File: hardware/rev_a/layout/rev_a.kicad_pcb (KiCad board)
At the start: 4 copper layers, 78 x 58 mm, 68 parts, among them J1 TSW-110-07-T-D, J2 TSW-110-07-T-D, U1 ADS1299-4PAGR, U2 TPS7A2033PDBVR

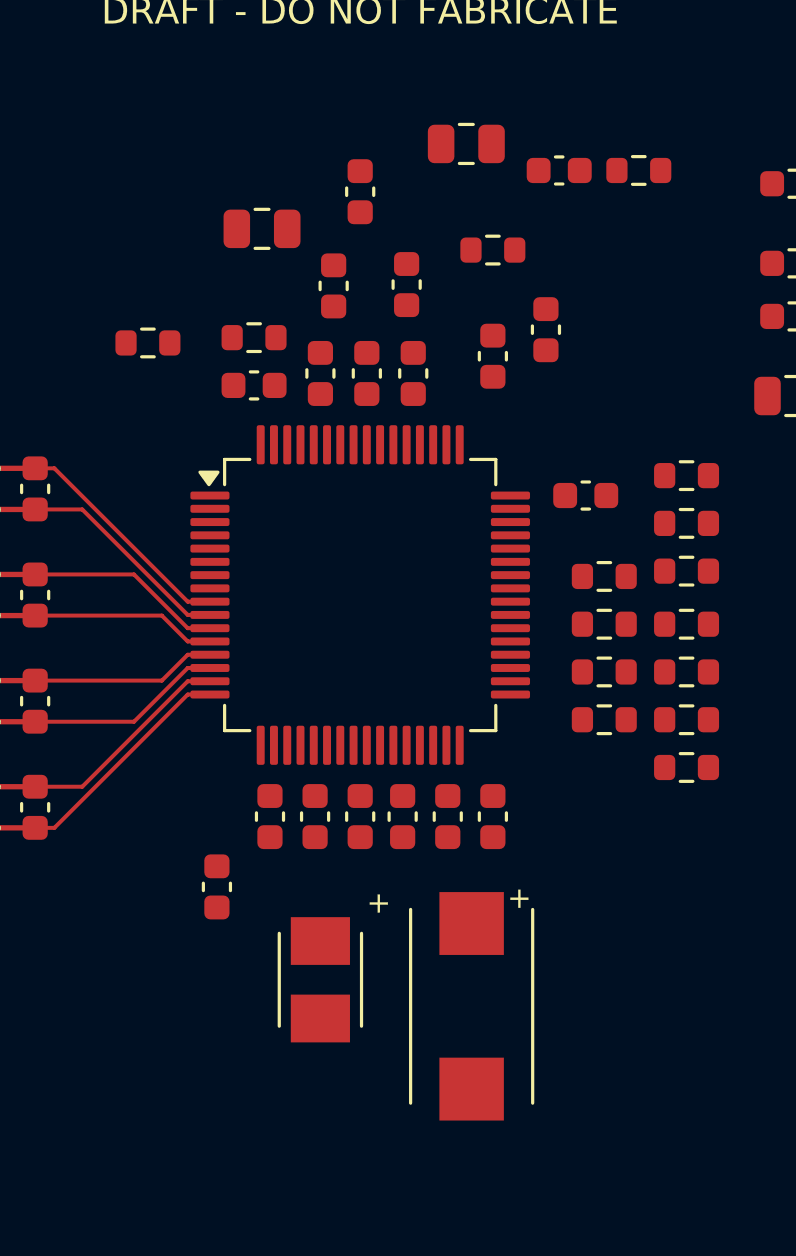
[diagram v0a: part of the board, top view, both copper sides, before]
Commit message: feat(hardware): route local reference and VCAP capacitor networks
Complete the five sensitive positive nets on front copper and add explicit local capacitor return traces. Preserve existing ADC-side routing, schematic, BOM and all approval flags. Two previously unrouted capacitors move for locality/clearance. Native cut-trace and cut-return controls pass; the full local gate remains to be executed on this commit. This is reconstructed local history, not a published GitHub head.
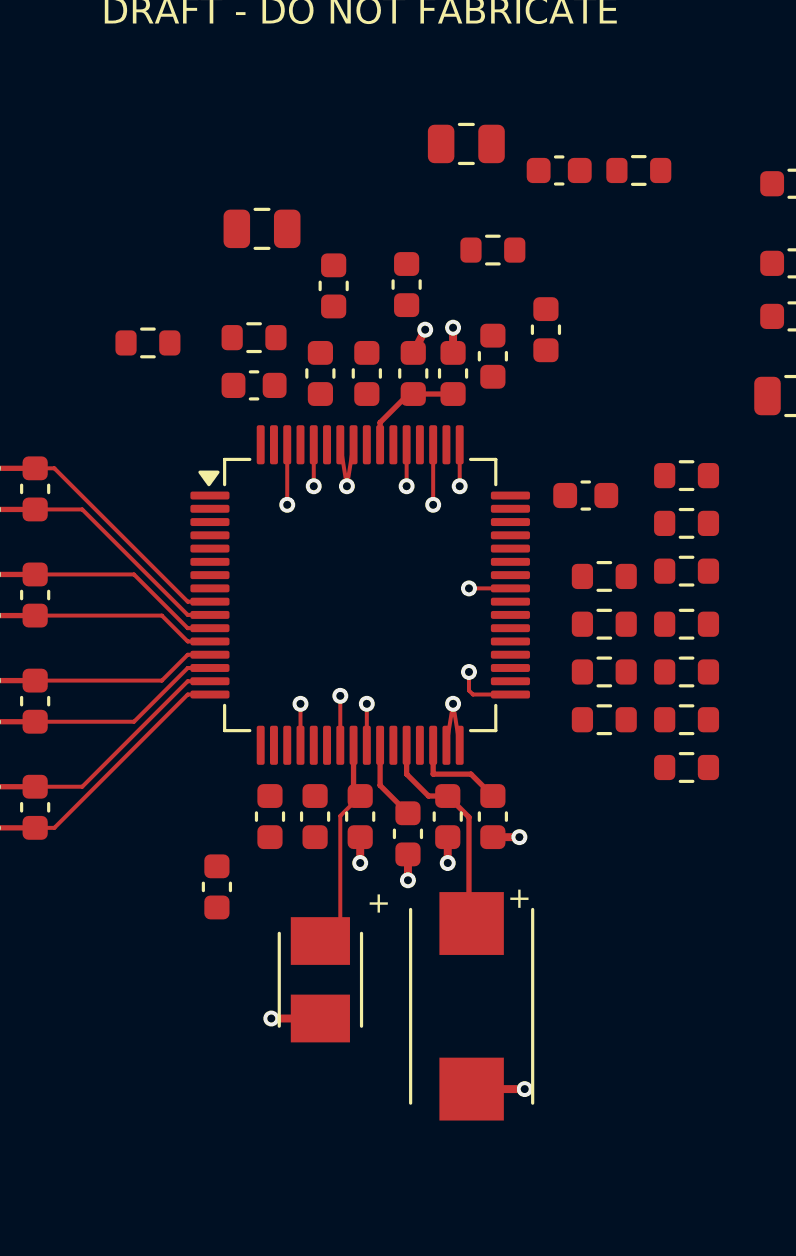
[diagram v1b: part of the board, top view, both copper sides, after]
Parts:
- moved C24 7.69 mm to (51.5, 28.6)
- moved C10 0.68 mm to (49.8, 46.0)
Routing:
- net GND: track 0.00 -> 158.7 mm, vias 0 -> 20
- net VCAP1: track 0.00 -> 8.16 mm
- net VREFP: track 0.00 -> 8.10 mm
- net VCAP3: track 0.00 -> 4.03 mm
- net VCAP2: track 0.00 -> 3.68 mm
- net VCAP4: track 0.00 -> 3.00 mm

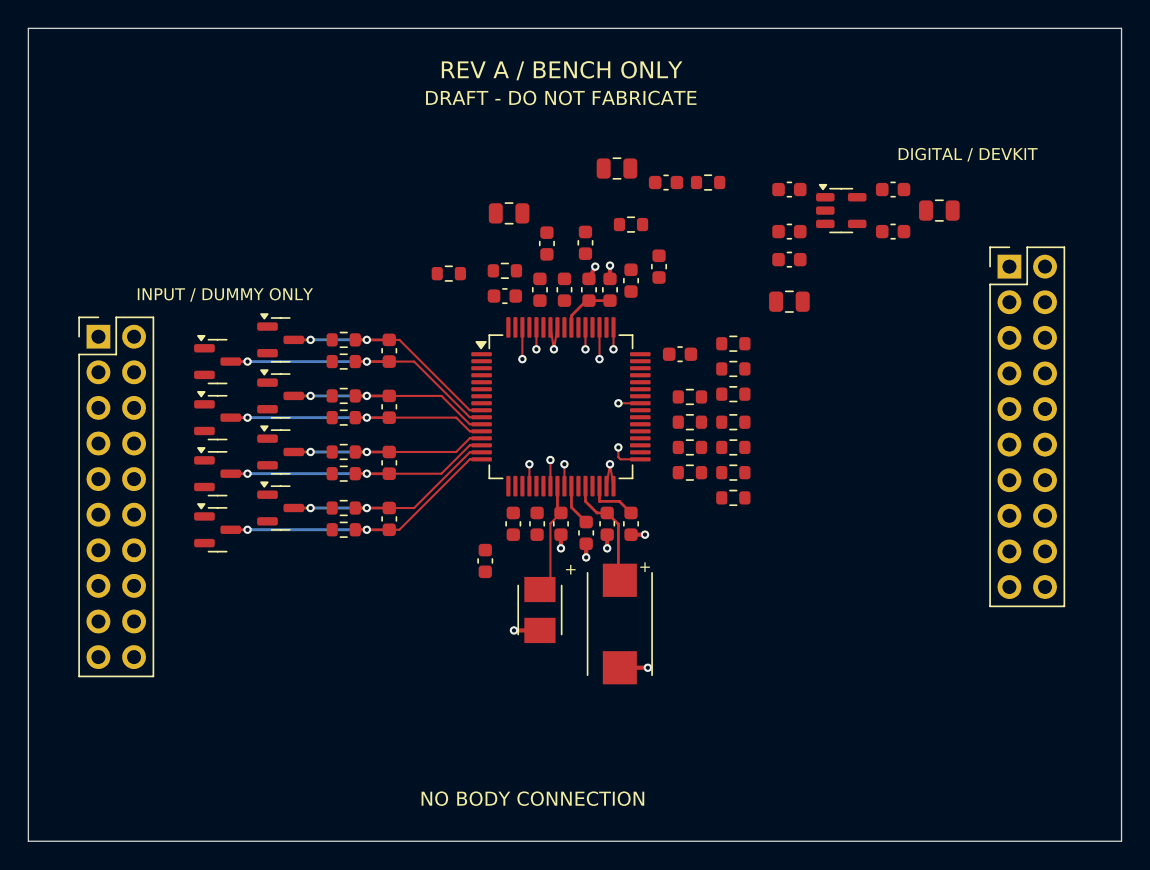
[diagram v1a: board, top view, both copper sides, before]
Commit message: feat(hardware): connect native ground plane and supply routes
Rebuild only the missing post-reference routing: one actual KiCad-filled In1 ground region and distinct VIN, AVDD and DVDD routes. Preserve all component data and existing copper. Canonical native DRC has zero parity/other findings and 35 deliberately unfinished connections. Require actual refill before testing each mutated board, reject missing/clipped planes and cut supply traces, and bind the new test source in the existing snapshot. No physical, purchasing, BOM, circuit, firmware, model or dependency change; full final local gate follows on this commit.
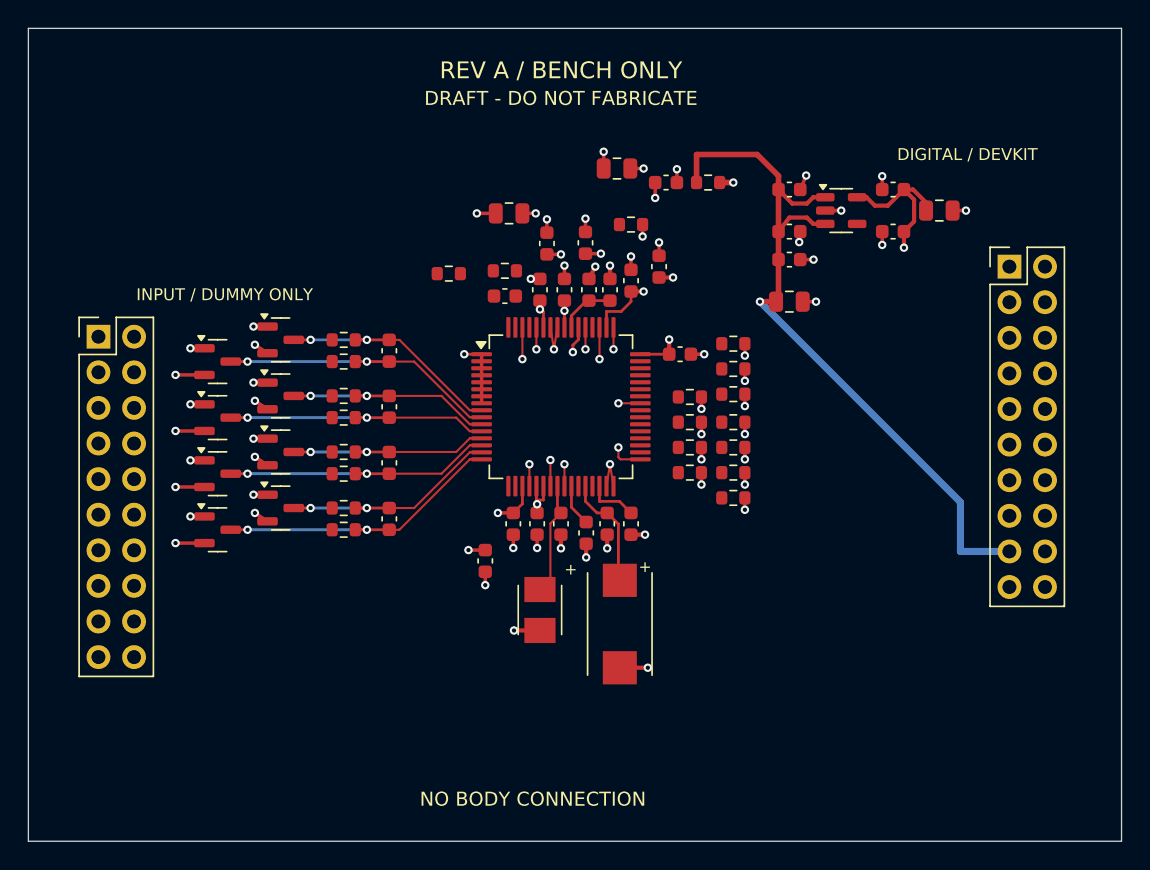
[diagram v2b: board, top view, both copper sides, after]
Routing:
- net AVDD: track 0.00 -> 244.6 mm, vias 0 -> 21
- net VIN_5V_AFE: track 0.00 -> 54.0 mm, vias 0 -> 1
- net DVDD: track 0.00 -> 49.7 mm, vias 0 -> 4
- net GND: track 158.7 -> 196.6 mm, vias 20 -> 61
- added copper zone on In1.Cu, net GND

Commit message: feat(hardware): complete the remaining PCB signal routing draft
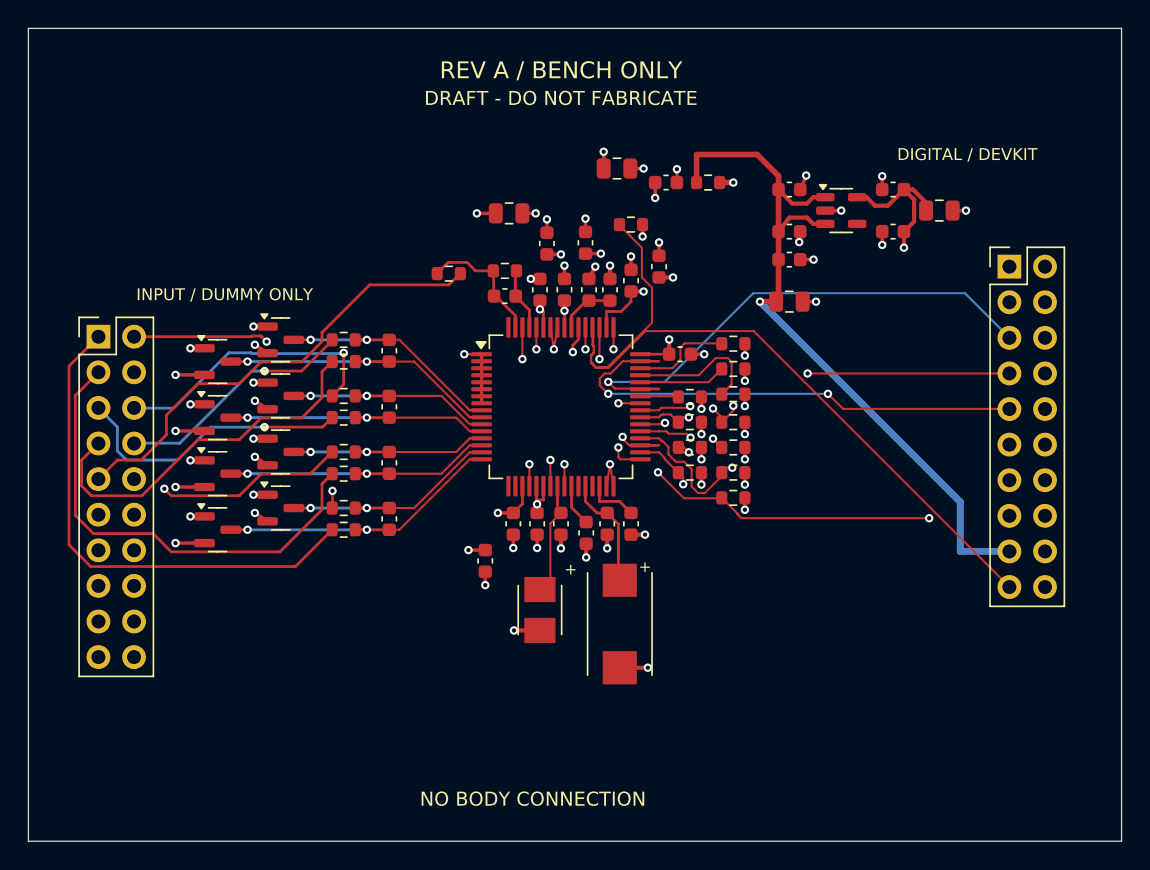
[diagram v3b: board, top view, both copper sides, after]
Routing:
- net CLKSEL: track 0.00 -> 57.7 mm
- net MISO: track 0.00 -> 37.7 mm, vias 0 -> 1
- net DRDY: track 0.00 -> 36.5 mm, vias 0 -> 2
- net CH1P_DUMMY: track 0.00 -> 36.3 mm
- net PWDN: track 0.00 -> 34.4 mm, vias 0 -> 3
- net CH2P_DUMMY: track 0.00 -> 33.8 mm
- net START: track 0.00 -> 33.8 mm, vias 0 -> 2
- net BIAS_AFTER_1M_DUMMY: track 0.00 -> 33.1 mm
- net MOSI: track 0.00 -> 33.0 mm, vias 0 -> 1
- net SCLK: track 0.00 -> 32.3 mm, vias 0 -> 3
- net RESET: track 0.00 -> 30.6 mm, vias 0 -> 1
- net CS: track 0.00 -> 28.1 mm, vias 0 -> 2
- net CH4P_DUMMY: track 0.00 -> 26.9 mm
- net CH1N_DUMMY: track 0.00 -> 23.5 mm, vias 0 -> 2
- net CH2N_DUMMY: track 0.00 -> 22.8 mm, vias 0 -> 1
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
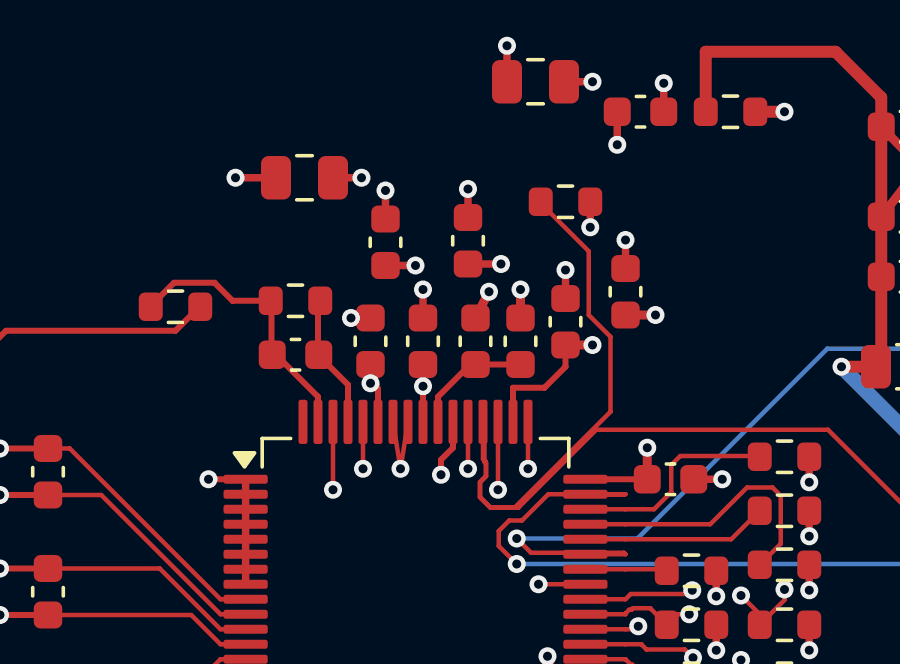
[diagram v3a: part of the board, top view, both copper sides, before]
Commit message: fix(pcb): provide direct local AVDD1 bypass and return paths
Move five existing capacitors, preserving their electrical identities and the other 63 footprint forms. Four AVDD1 front paths now pass the preceding native failures. Fresh all-severity parity/DRC is 0/0/0. Two reconnection controls preserve general DRC/connectivity but fail the direct local paths; benign track subdivision remains accepted. VCAP3 paths stay front-only, with the longer HF path and AVDD56 tradeoff to be documented explicitly; no performance or approval claim.
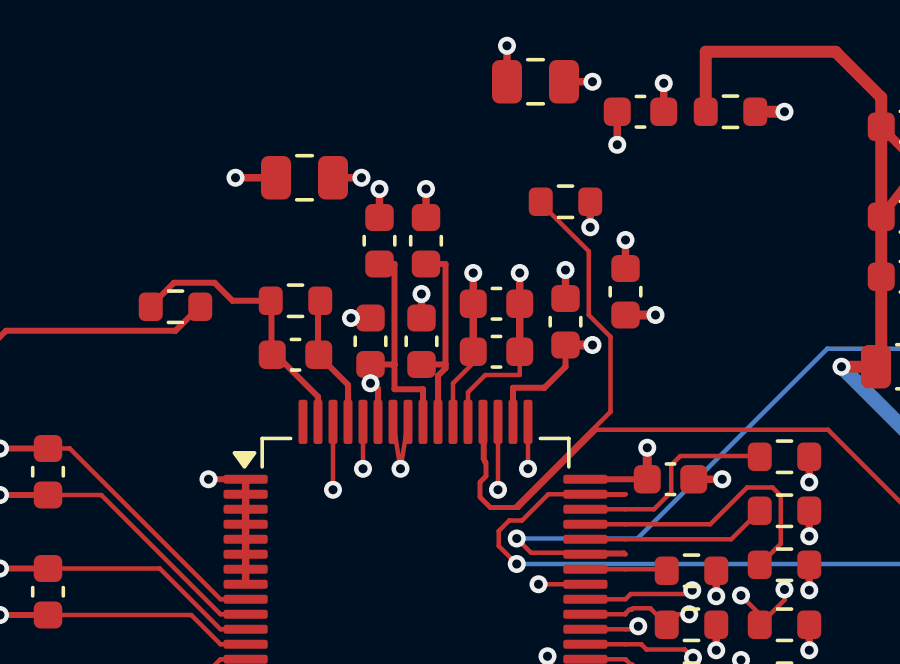
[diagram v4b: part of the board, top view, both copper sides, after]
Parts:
- moved C24 4.60 mm to (48.4, 25.3)
- moved C27 4.23 mm to (50.7, 27.4), turned to 0 degrees
- moved C16 3.82 mm to (50.7, 29.0), turned to 0 degrees
- moved C14 3.65 mm to (46.8, 25.3)
- moved C9 1.80 mm to (48.2, 28.6)
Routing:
- net GND: track 196.6 -> 186.4 mm, vias 61 -> 59
- net AVDD: track 244.6 -> 241.2 mm, vias 21 -> 18
- net VCAP3: track 4.03 -> 6.82 mm
